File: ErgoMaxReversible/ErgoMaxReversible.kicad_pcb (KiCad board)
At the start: 2 copper layers, 182.8 x 169.2 mm, 102 parts, among them J1 PJ-320A, K1 KEYSW, K10 KEYSW, K11 KEYSW, K12 KEYSW, K13 KEYSW, K14 KEYSW, K15 KEYSW, K16 KEYSW, K17 KEYSW, K18 KEYSW, K19 KEYSW, K2 KEYSW, K20 KEYSW, K21 KEYSW, K22 KEYSW, K23 KEYSW, K24 KEYSW, K25 KEYSW, K26 KEYSW, K27 KEYSW, K28 KEYSW, K29 KEYSW, K3 KEYSW, K30 KEYSW, K31 KEYSW, K32 KEYSW, K33 KEYSW, K34 KEYSW, K35 KEYSW, K36 KEYSW, K37 KEYSW, K38 KEYSW, K39 KEYSW, K4 KEYSW, K40 KEYSW, K41 KEYSW, K42 KEYSW, K43 KEYSW, K44 KEYSW, K5 KEYSW, K6 KEYSW, K7 KEYSW, K8 KEYSW, K9 KEYSW, U1 ProMicro

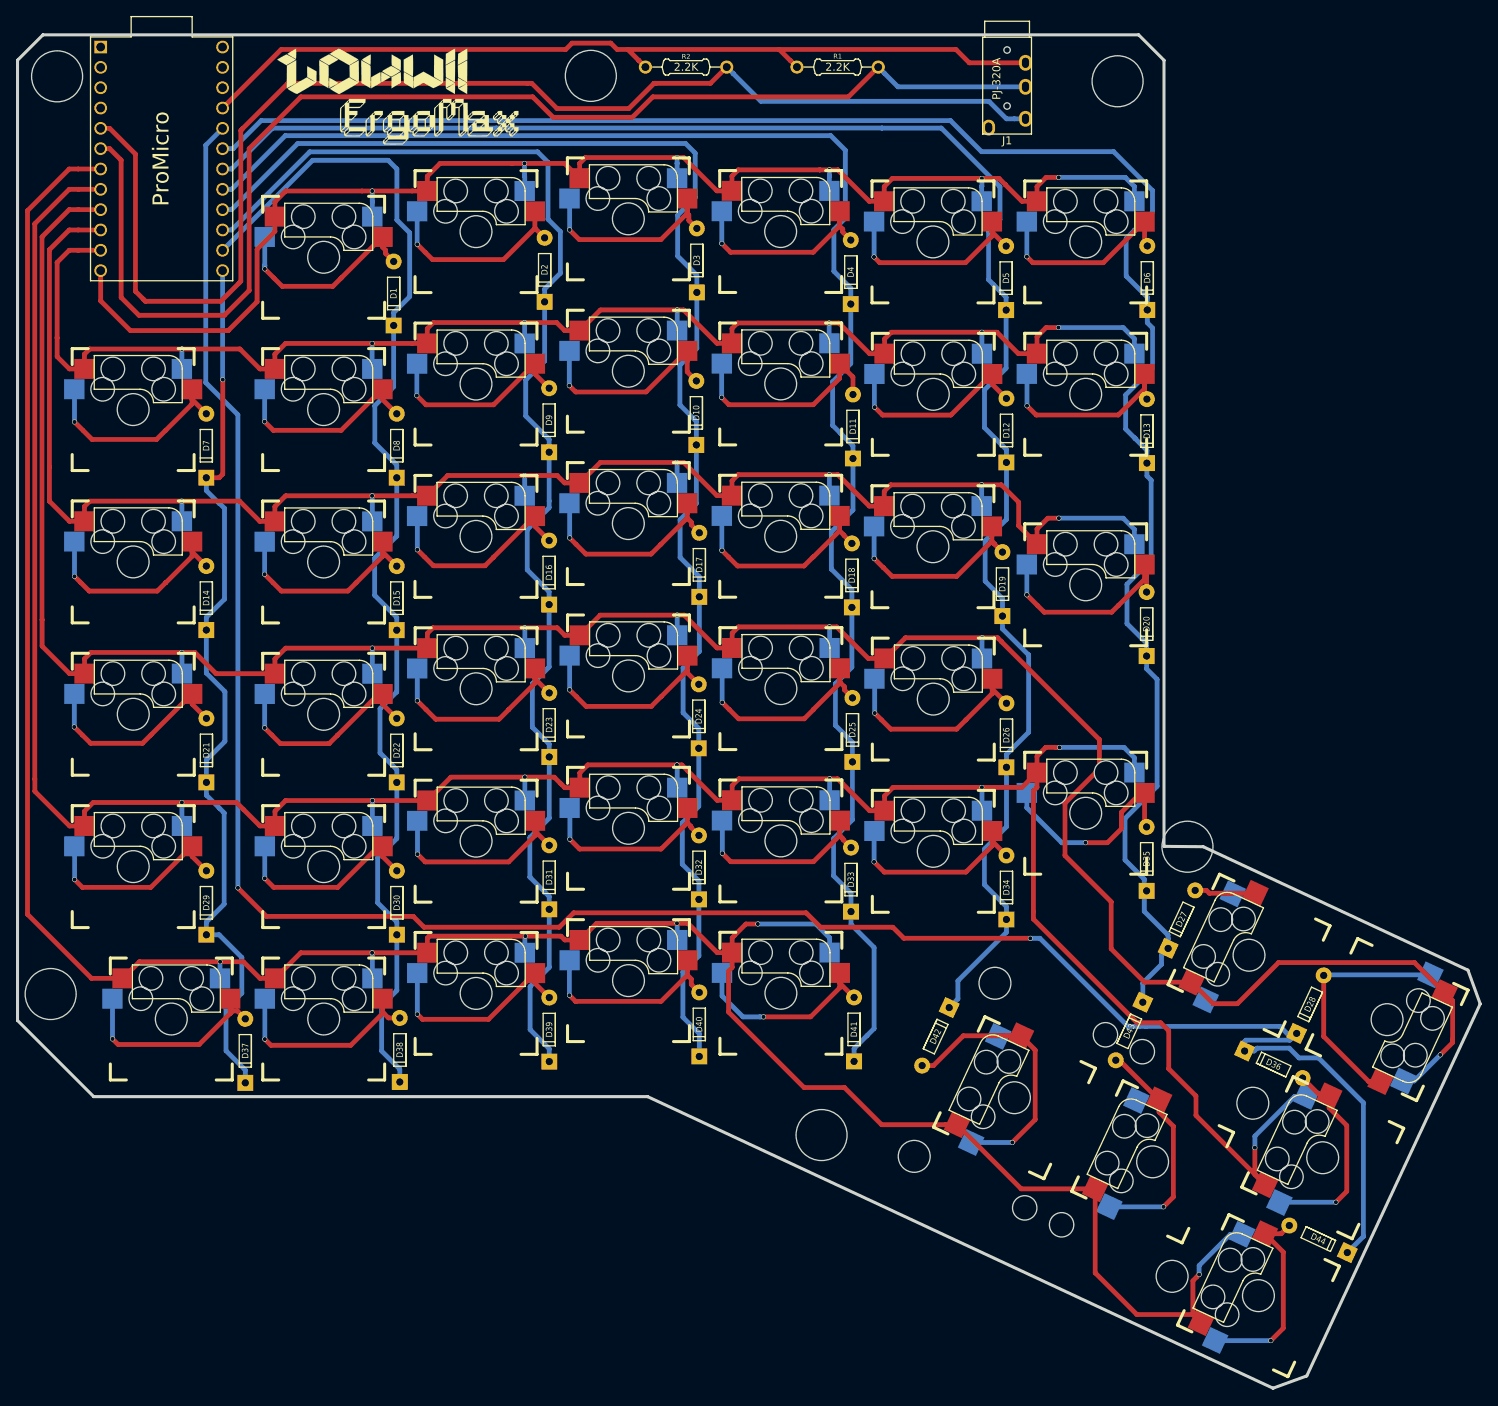
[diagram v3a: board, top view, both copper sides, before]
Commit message: improve wiring on reversible PCB
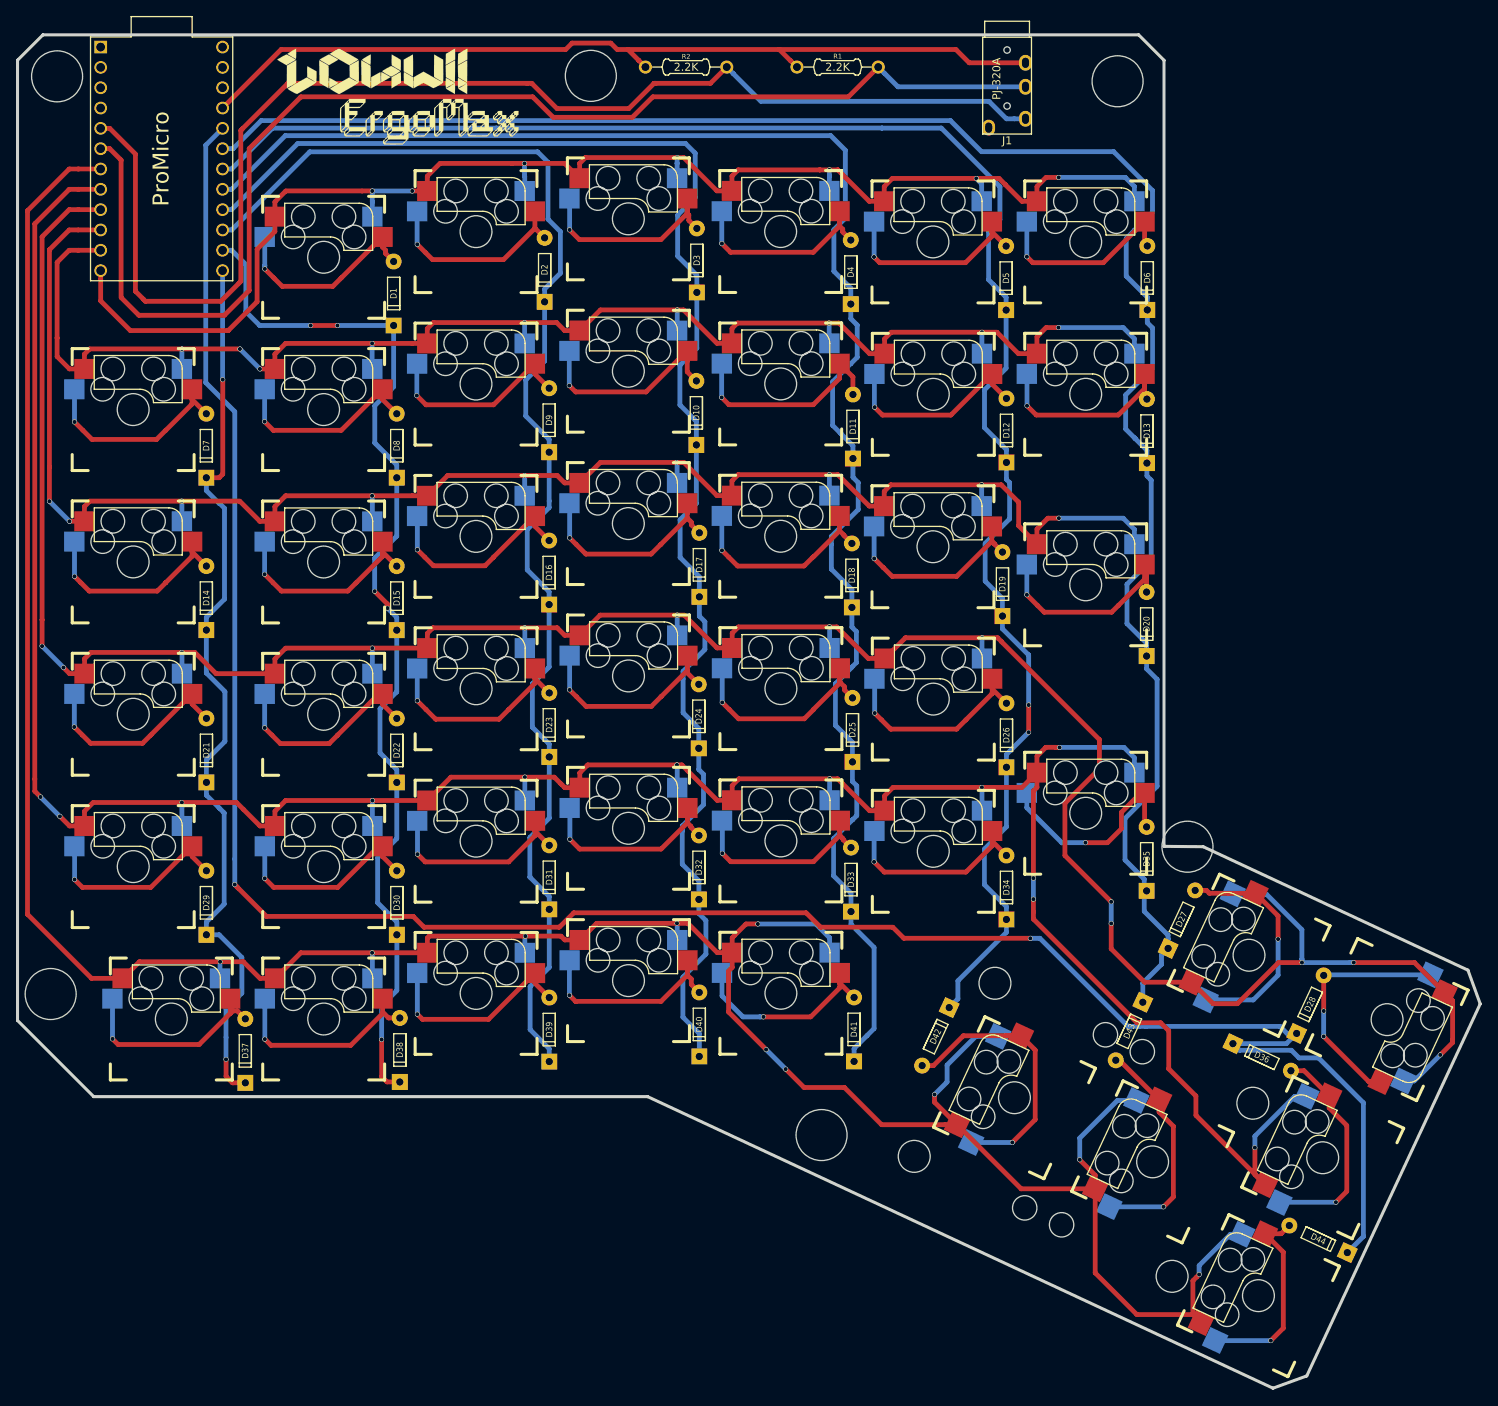
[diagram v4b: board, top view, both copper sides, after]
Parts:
- moved D36 1.73 mm to (265.9, 163.6)
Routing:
- net /Row5: track 327.4 -> 360.7 mm, vias 6 -> 10
- net Net-(D27-Pad2): track 7.69 -> 29.4 mm, vias 0 -> 1
- net /Col1: track 152.4 -> 134.1 mm, vias 0 -> 5
- net /Row3: track 324.1 -> 338.7 mm, vias 7 -> 13
- net Net-(D36-Pad2): track 26.1 -> 29.0 mm
- net /Col7: track 284.4 -> 286.9 mm
- net /Col4: track 207.0 -> 209.2 mm
- net /Col3: track 186.4 -> 188.2 mm
- net /Col0: track 113.6 -> 114.5 mm, vias 1 -> 2
- net /Col5: track 218.5 -> 218.8 mm, vias 0 -> 2
- net /Row0: track 181.5 -> 181.9 mm, vias 6 -> 7
- net /Row2: vias 7 -> 9
- net Net-(D28-Pad2): vias 0 -> 2
- net /Row4: vias 8 -> 12
- net /Row1: vias 7 -> 9

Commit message: finish and improve reversible PCB
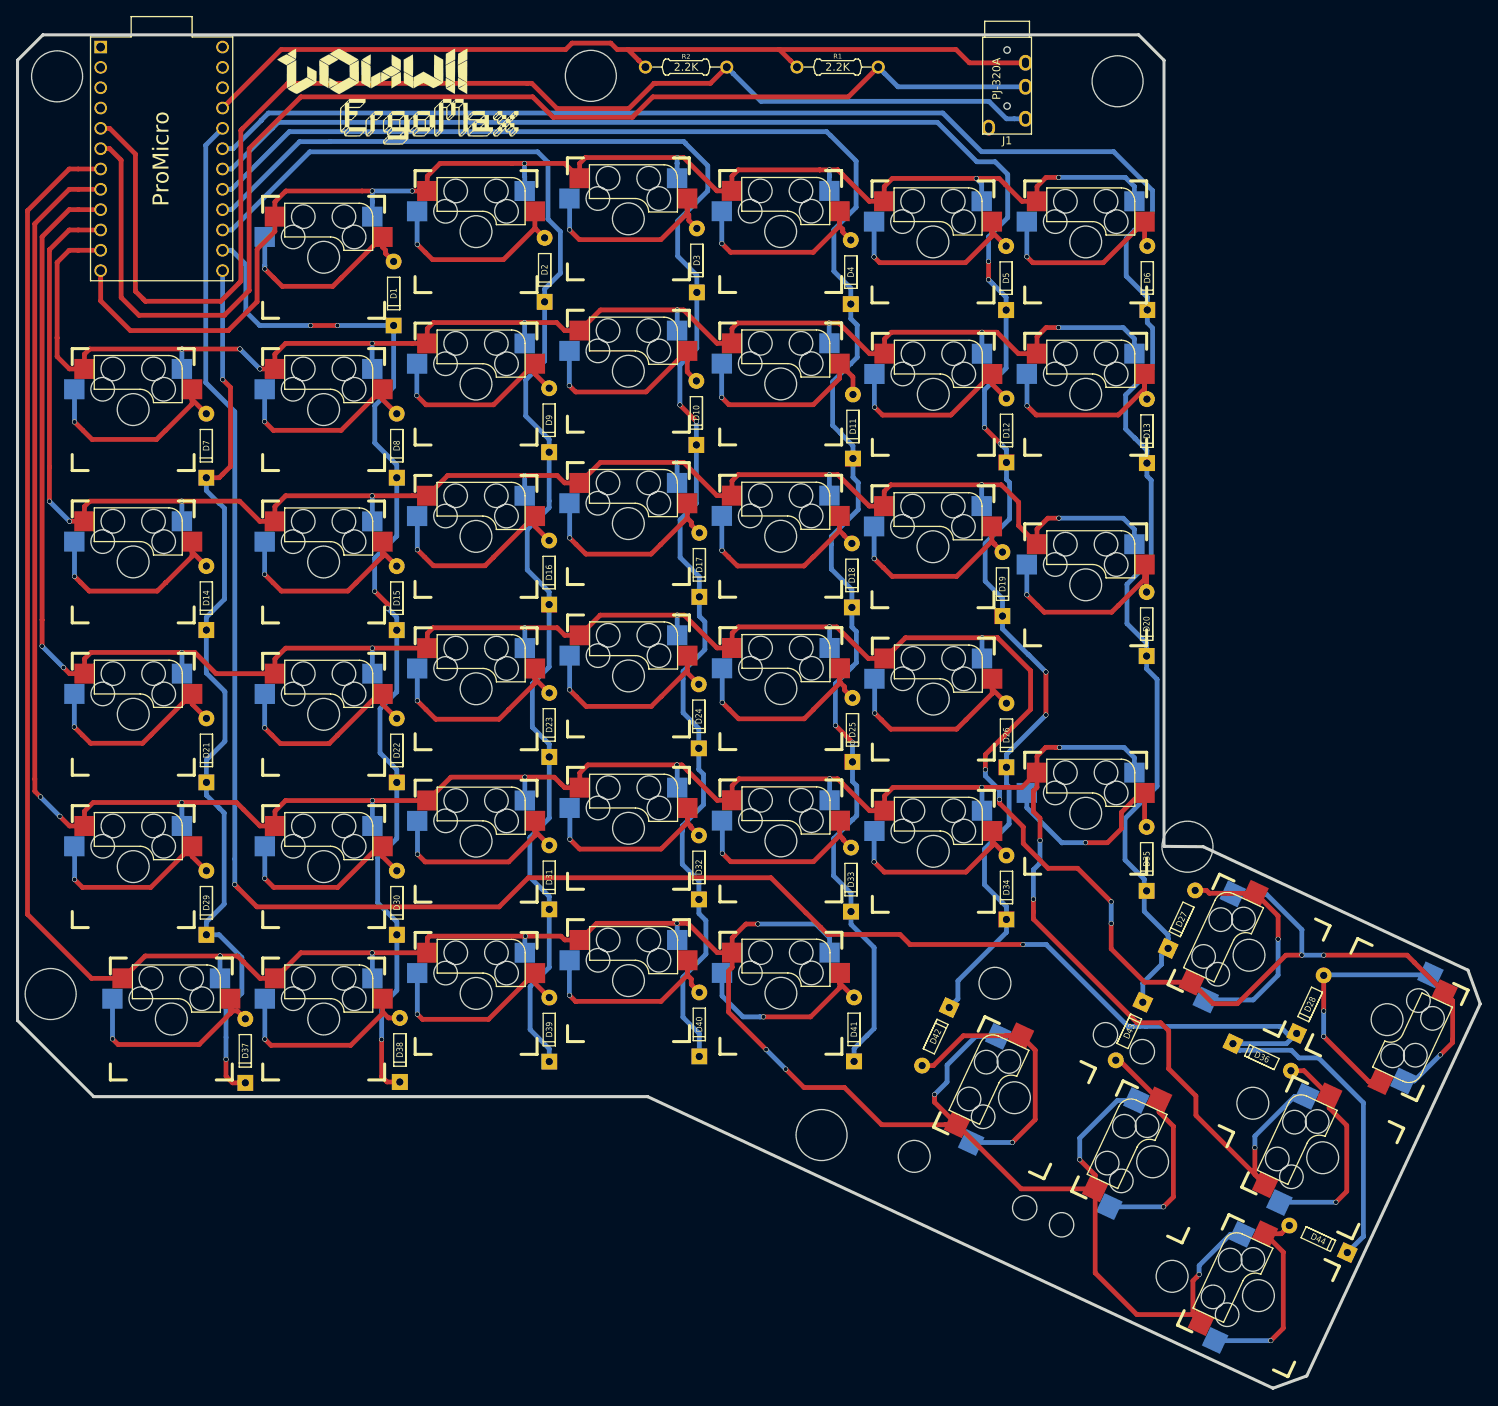
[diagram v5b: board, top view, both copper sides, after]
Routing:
- net /Col5: track 218.8 -> 225.4 mm, vias 2 -> 6
- net /Row3: track 338.7 -> 341.8 mm, vias 13 -> 15
- net /Col3: track 188.2 -> 189.8 mm, vias 0 -> 2
- net /Col7: track 286.9 -> 288.4 mm
- net /Col4: track 209.2 -> 210.7 mm, vias 0 -> 2
- net /Row5: track 360.7 -> 362.0 mm
- net /Col6: track 236.8 -> 237.6 mm
- net /Col0: track 114.5 -> 115.3 mm
- net /Row4: track 341.9 -> 342.5 mm

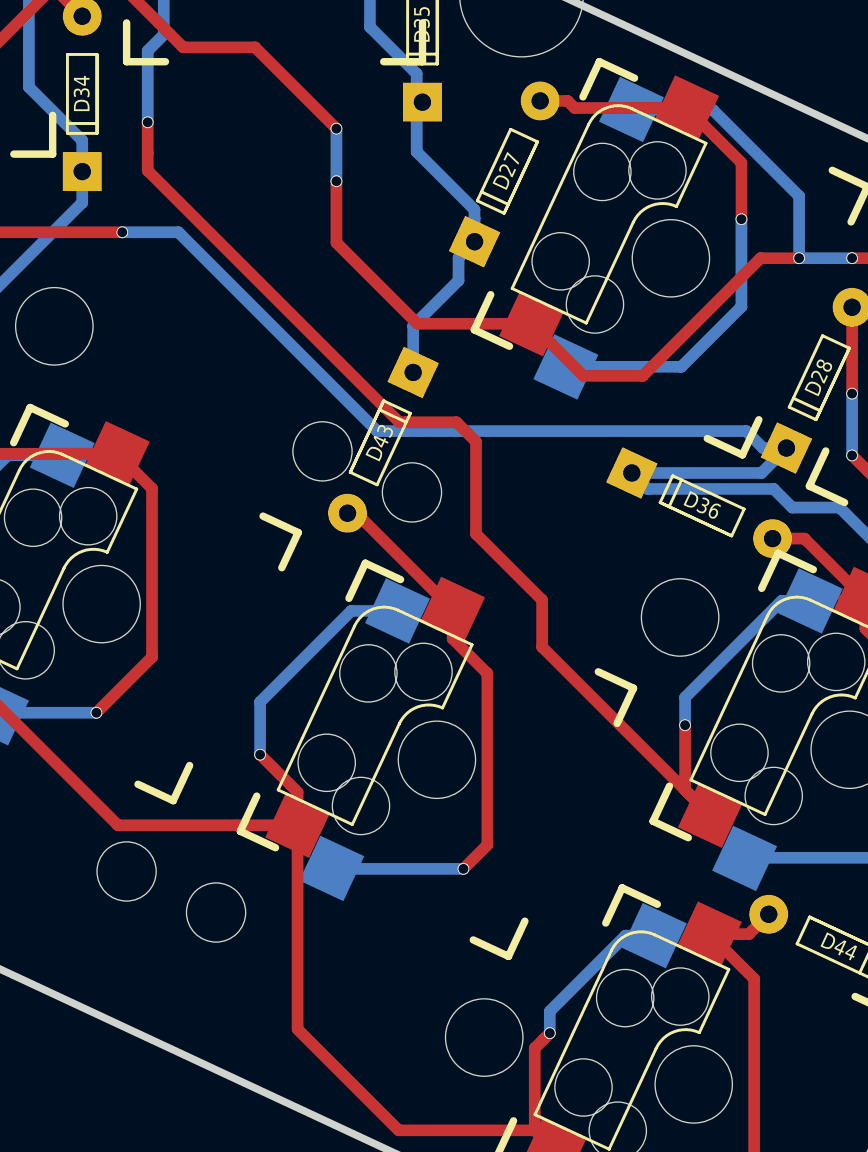
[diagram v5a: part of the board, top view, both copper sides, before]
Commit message: more improvements on reversible pcb
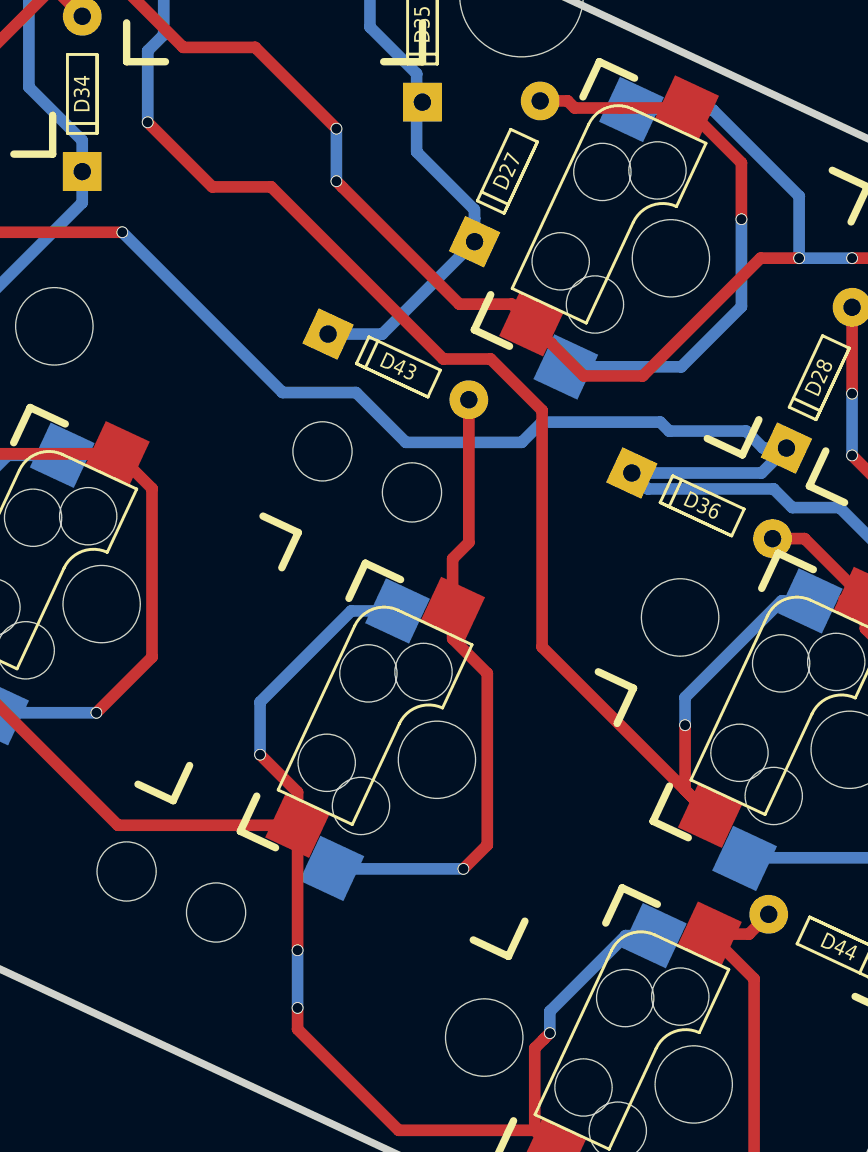
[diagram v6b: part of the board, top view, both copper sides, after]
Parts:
- moved D43 4.02 mm to (250.2, 156.5), turned to 155 degrees
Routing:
- net Net-(D43-Pad2): track 28.9 -> 32.5 mm
- net /Row3: track 341.8 -> 340.0 mm
- net /Row4: track 342.5 -> 344.0 mm
- net /Col6: track 237.6 -> 239.1 mm
- net /Col7: track 288.4 -> 289.2 mm
- net /Row5: vias 10 -> 12
